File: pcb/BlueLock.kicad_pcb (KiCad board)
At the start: 2 copper layers, 47.7 x 22 mm, 47 parts, among them J1 USB_B_Micro, J2 Load, M1 Motor_DC, Q1 Q_NMOS_GSD, Q2 Q_PMOS_GSD, Q3 Q_NMOS_GSD, Q4 Q_PMOS_GSD, Q5 Q_NMOS_GSD, Q6 Q_NMOS_GSD, SW1 SW_Push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

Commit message: 更新pcb
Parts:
- removed the 0 at (108.7, 70.6)
- removed the 0 at (108.7, 87.2)
- removed the 0 at (66.3, 87.2)
- removed the 0 at (66.3, 70.6)
- removed C8: 10uf, Capacitor_SMD:C_0603_1608Metric
- removed R14: 1k, Resistor_SMD:R_0603_1608Metric
- removed R17: 1R, Resistor_SMD:R_0805_2012Metric
- added 0: R2R4, MyFoot:R2R4, F.Cu at (53.5, 86.6)
- added 0: R2R4, MyFoot:R2R4, F.Cu at (53.5, 70.0)
- added 0: R2R4, MyFoot:R2R4, F.Cu at (95.8, 70.0)
- added 0: R2R4, MyFoot:R2R4, F.Cu at (95.8, 86.6)
- added C9: 0.1uf, Capacitor_SMD:C_0603_1608Metric, F.Cu at (53.4, 76.5)
- added R12: 1K, Resistor_SMD:R_0603_1608Metric, F.Cu at (53.4, 78.0)
- added R13: 1k, Resistor_SMD:R_0603_1608Metric, F.Cu at (77.7, 81.8)
- added U5: XB3306A, Package_TO_SOT_SMD:SOT-23, F.Cu at (53.1, 73.9)
- BT1, M1: footprint Connector_PinHeader_2.54mm:PinHeader_1x02_P2.54mm_Vertical -> Custom:Pin_2_wide
- C2: footprint Capacitor_SMD:C_0603_1608Metric -> Capacitor_SMD:C_1206_3216Metric
- D1: value LED_RBAG -> RGB_1209; footprint LED_SMD:LED_Kingbright_AAA3528ESGCT -> Custom:RGB_1209
- D2: footprint Diode_SMD:D_SOD-323 -> Diode_SMD:D_SOD-123
- R2: value 20k -> 100k
- R3: value 165k -> 750k
- SW1: footprint Button_Switch_SMD:SW_Push_1P1T_NO_CK_KSC6xxJ -> Custom:SW_6x6
- moved BT1 56.7 mm to (52.6, 81.5)
- moved J2 50.1 mm to (57.8, 69.5), turned to 0 degrees
- moved C3 48.1 mm to (57.9, 85.0), turned to 180 degrees
- moved U4 47.3 mm to (57.7, 82.4), turned to 270 degrees
- moved C4 47.0 mm to (57.6, 79.9), turned to 0 degrees
- moved C6 43.2 mm to (61.2, 87.0), turned to 90 degrees
- moved R4 39.8 mm to (63.5, 88.0), turned to 0 degrees
- moved R5 38.2 mm to (63.5, 86.1), turned to 180 degrees
- moved U1 32.4 mm to (67.3, 87.1), turned to 0 degrees
- moved M1 31.0 mm to (96.8, 78.1), turned to 180 degrees
- moved R9 29.2 mm to (92.1, 69.0), turned to 180 degrees
- moved R10 29.0 mm to (95.1, 82.2), turned to 180 degrees
- moved U3 28.9 mm to (66.8, 76.3), turned to 0 degrees
- moved RX1 27.8 mm to (67.6, 81.8), turned to 180 degrees
- moved R1 27.8 mm to (70.2, 87.4), turned to 270 degrees
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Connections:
- BT1 pad 2: GND -> /B-
- Q3 pad 2: /CHK_I -> GND
- Q5 pad 2: /CHK_I -> GND
- R15 pad 1: Net-(D1-Pad1) -> Net-(D1-Pad4)
- R15 pad 2: /LEDR -> /LEDB
- R16 pad 1: Net-(D1-Pad2) -> Net-(D1-Pad1)
- R16 pad 2: /LEDB -> /LEDR
- U1 pad 5: /STDBY -> /LEDG
- U3 pad 10: /CHRG -> /LEDR
- U3 pad 18: /BT -> Net-(U3-Pad18)
- U3 pad 3: /CHK_I -> /H2
- U3 pad 6: /LEDR -> /BT
- U3 pad 7: /H2 -> /CHRG
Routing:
- net /CHK_I: track 37.3 -> 0.00 mm, vias 2 -> 0
- net /LEDR: track 23.0 -> 4.82 mm, vias 2 -> 0
- net /STDBY: track 16.7 -> 0.00 mm, vias 2 -> 0
- net /LEDG: track 0.00 -> 14.4 mm
- net /BT: track 54.9 -> 42.9 mm
- net GND: track 117.6 -> 129.4 mm, vias 44 -> 47
- net /B-: track 0.00 -> 6.29 mm
- net Net-(C9-Pad1): track 0.00 -> 5.14 mm
- net +BATT: track 58.7 -> 54.6 mm, vias 3 -> 4
- net /H2: track 29.0 -> 31.7 mm
- net Net-(D1-Pad2): track 7.87 -> 5.57 mm
- net Net-(D1-Pad1): track 2.55 -> 4.62 mm
- net Net-(D1-Pad4): track 6.77 -> 8.54 mm, vias 0 -> 2
- net /CLK: track 41.4 -> 39.6 mm
- net /VDD: track 50.8 -> 49.4 mm, vias 6 -> 4
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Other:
- board size 47.7 x 22 mm -> 47.7 x 22.8 mm
- board text added: "B+"
- board text added: "B-"
- board text added: "V C D G"

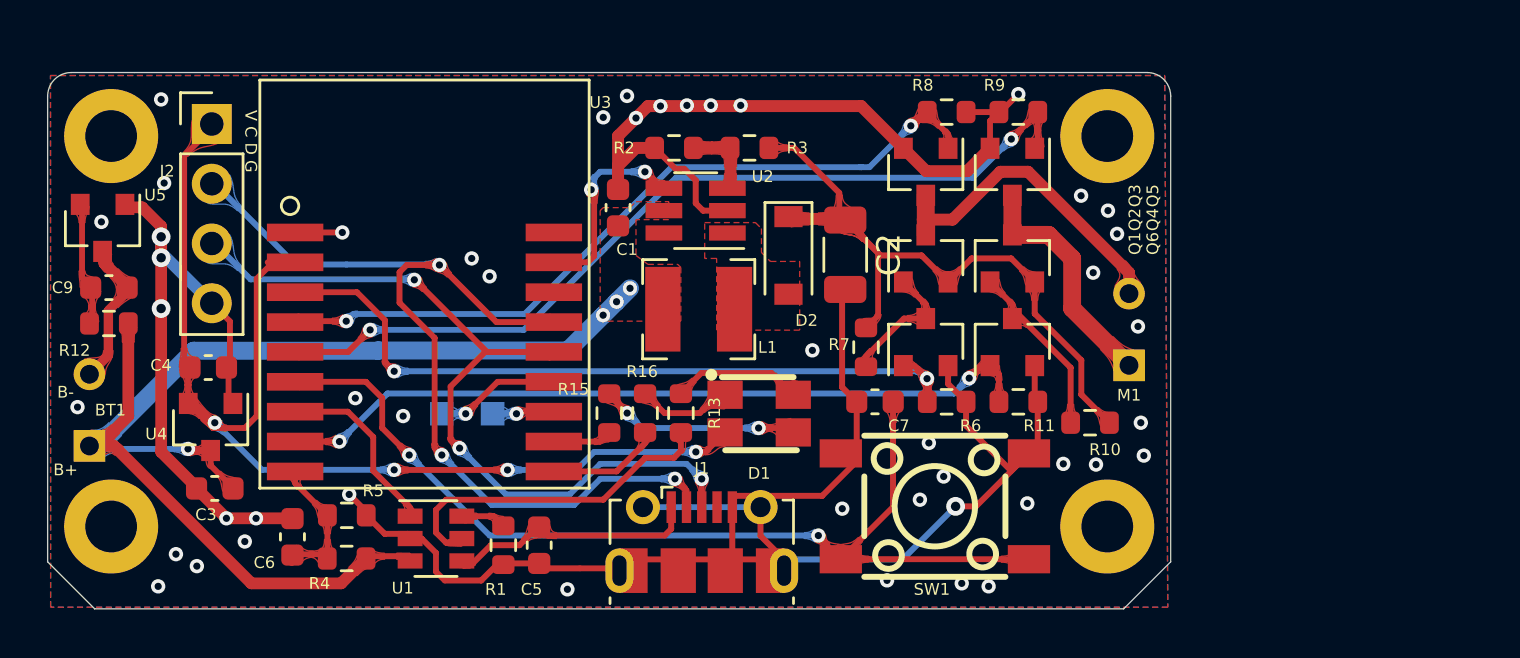
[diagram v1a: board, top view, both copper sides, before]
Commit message: 单电池,不升压版本.
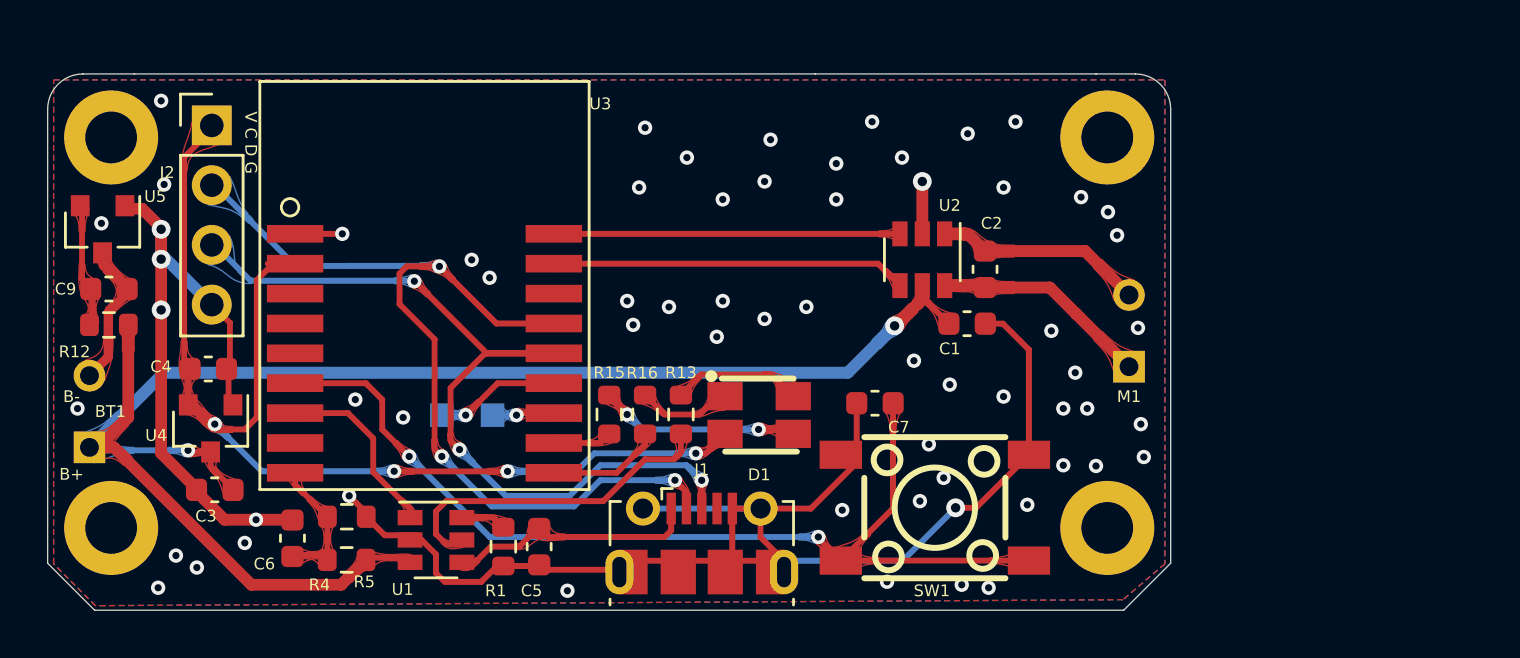
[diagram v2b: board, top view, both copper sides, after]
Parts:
- removed the 0 at (53.5, 86.6)
- removed the 0 at (53.5, 70.0)
- removed the 0 at (95.8, 70.0)
- removed the 0 at (95.8, 86.6)
- removed D2: D_Schottky, Diode_SMD:D_SOD-123
- removed L1: 3.3uH, Inductor_SMD:L_Bourns-SRN4018
- removed Q1, Q3, Q5, Q6: Q_NMOS_GSD, Package_TO_SOT_SMD:SOT-23
- removed Q2, Q4: Q_PMOS_GSD, Package_TO_SOT_SMD:SOT-23
- removed R10, R7: 1k, Resistor_SMD:R_0603_1608Metric
- removed R11, R6, R8, R9: 10k, Resistor_SMD:R_0603_1608Metric
- removed R2: 100k, Resistor_SMD:R_0603_1608Metric
- removed R3: 750k, Resistor_SMD:R_0603_1608Metric
- added 0: R2R4, MyFoot:R2R4, F.Cu at (53.5, 86.7)
- added 0: R2R4, MyFoot:R2R4, F.Cu at (53.5, 70.1)
- added 0: R2R4, MyFoot:R2R4, F.Cu at (95.8, 86.7)
- added 0: R2R4, MyFoot:R2R4, F.Cu at (95.8, 70.1)
- C1: value 22uf -> 0.1uf
- C2: value 22uf -> 0.1uf; footprint Capacitor_SMD:C_1206_3216Metric -> Capacitor_SMD:C_0603_1608Metric
- U2: value LN2220 -> FM116B; footprint Package_TO_SOT_SMD:SOT-23-6_Handsoldering -> Package_TO_SOT_SMD:SOT-23-6
- moved C1 15.8 mm to (90.7, 75.7), turned to 90 degrees
- moved U2 9.86 mm to (88.0, 75.3), turned to -90 degrees
- moved C2 5.95 mm to (89.9, 78.0), turned to 0 degrees
- moved C3 0.06 mm to (57.9, 85.1)
- moved C4 0.06 mm to (57.6, 79.9)
- moved C5 0.06 mm to (71.7, 87.5)
- moved C7 0.06 mm to (86.0, 81.4)
- moved C9 0.06 mm to (53.4, 76.5)
- moved D1 0.06 mm to (81.0, 81.9)
- moved J1 0.06 mm to (78.6, 87.3)
- moved J2 0.06 mm to (57.8, 69.6)
- moved M1 0.06 mm to (96.8, 78.2)
- moved R1 0.06 mm to (70.2, 87.5)
- moved R12 0.06 mm to (53.4, 78.0)
- moved R13 0.06 mm to (77.7, 81.8)
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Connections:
- net /EN renamed /IN1
- C1 pad 1: GND -> Net-(C1-Pad1)
- C1 pad 2: +BATT -> Net-(C1-Pad2)
- C2 pad 1: /VBUS -> +BATT
- J1 pad 4: Net-(J1-Pad4) -> unconnected-(J1-Pad4)
- M1 pad 1: Net-(M1-Pad1) -> Net-(C1-Pad1)
- M1 pad 2: Net-(M1-Pad2) -> Net-(C1-Pad2)
- U2 pad 1: /SW -> Net-(C1-Pad2)
- U2 pad 3: /FB -> /IN2
- U2 pad 6: Net-(U2-Pad6) -> Net-(C1-Pad1)
- U3 pad 16: Net-(U3-Pad16) -> unconnected-(U3-Pad16)
- U3 pad 18: Net-(U3-Pad18) -> /IN2
- U3 pad 3: /H2 -> unconnected-(U3-Pad3)
- U3 pad 4: /L1 -> unconnected-(U3-Pad4)
- U3 pad 5: /L2 -> unconnected-(U3-Pad5)
- U3 pad 8: /H1 -> unconnected-(U3-Pad8)
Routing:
- net GND: track 129.4 -> 90.4 mm, vias 47 -> 64
- net /L2: track 37.4 -> 0.00 mm, vias 2 -> 0
- net /H1: track 32.6 -> 0.00 mm, vias 2 -> 0
- net /L1: track 32.5 -> 0.00 mm, vias 2 -> 0
- net /H2: track 31.7 -> 0.00 mm, vias 2 -> 0
- net /VBUS: track 29.2 -> 0.00 mm
- net +BATT: track 54.6 -> 69.9 mm, vias 4 -> 2
- net /IN2: track 0.00 -> 14.7 mm
- net Net-(M1-Pad2): track 13.8 -> 0.00 mm
- net Net-(M1-Pad1): track 10.4 -> 0.00 mm
- net Net-(C1-Pad1): track 0.00 -> 9.27 mm
- net Net-(C1-Pad2): track 0.00 -> 8.91 mm
- net Net-(Q4-Pad1): track 7.63 -> 0.00 mm
- net /IN1: track 8.87 -> 15.1 mm, vias 2 -> 0
- net Net-(Q1-Pad3): track 5.59 -> 0.00 mm
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- removed copper zone on F.Cu, net +BATT
- removed copper zone on F.Cu, net /SW
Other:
- outline, holes or cut-outs redrawn
- net class Default removed
